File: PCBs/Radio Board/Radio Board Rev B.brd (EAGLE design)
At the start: 95.9 x 90.2 mm, 10 parts

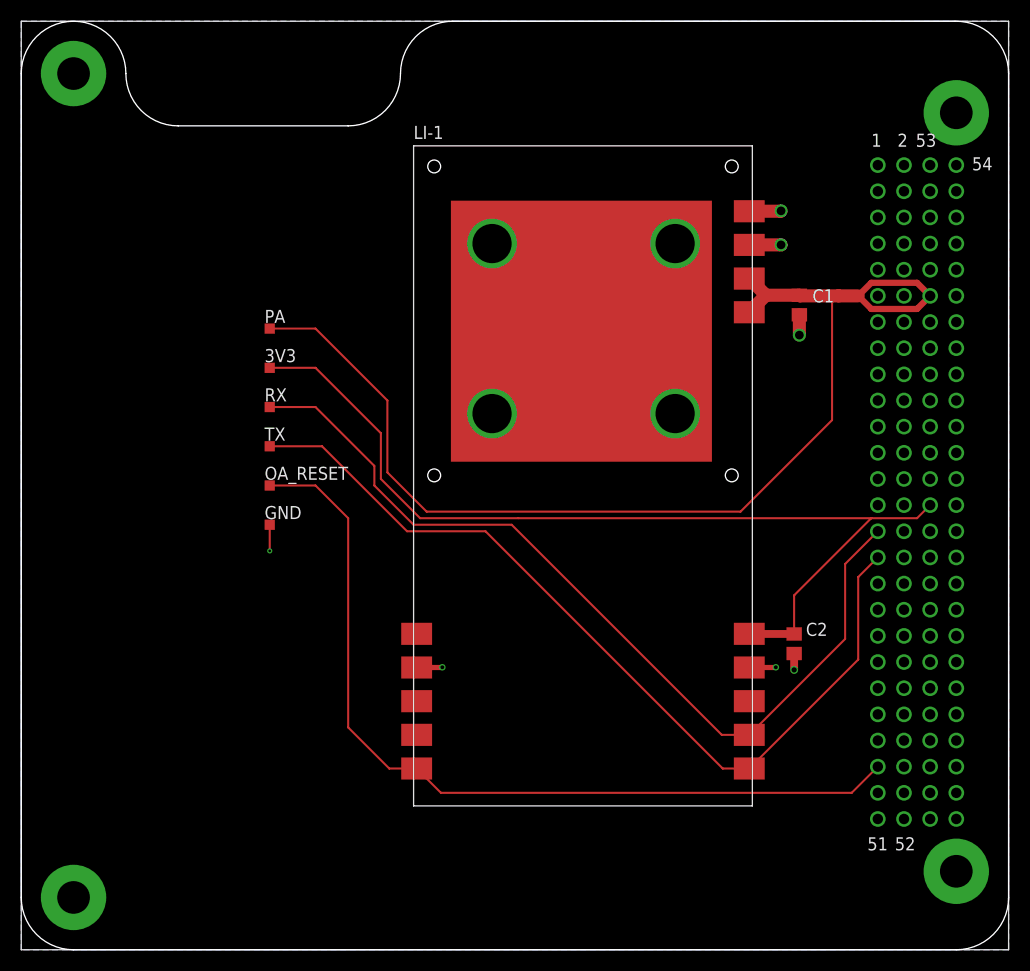
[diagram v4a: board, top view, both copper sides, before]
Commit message: Add Molex connector and connector bypass to radio board
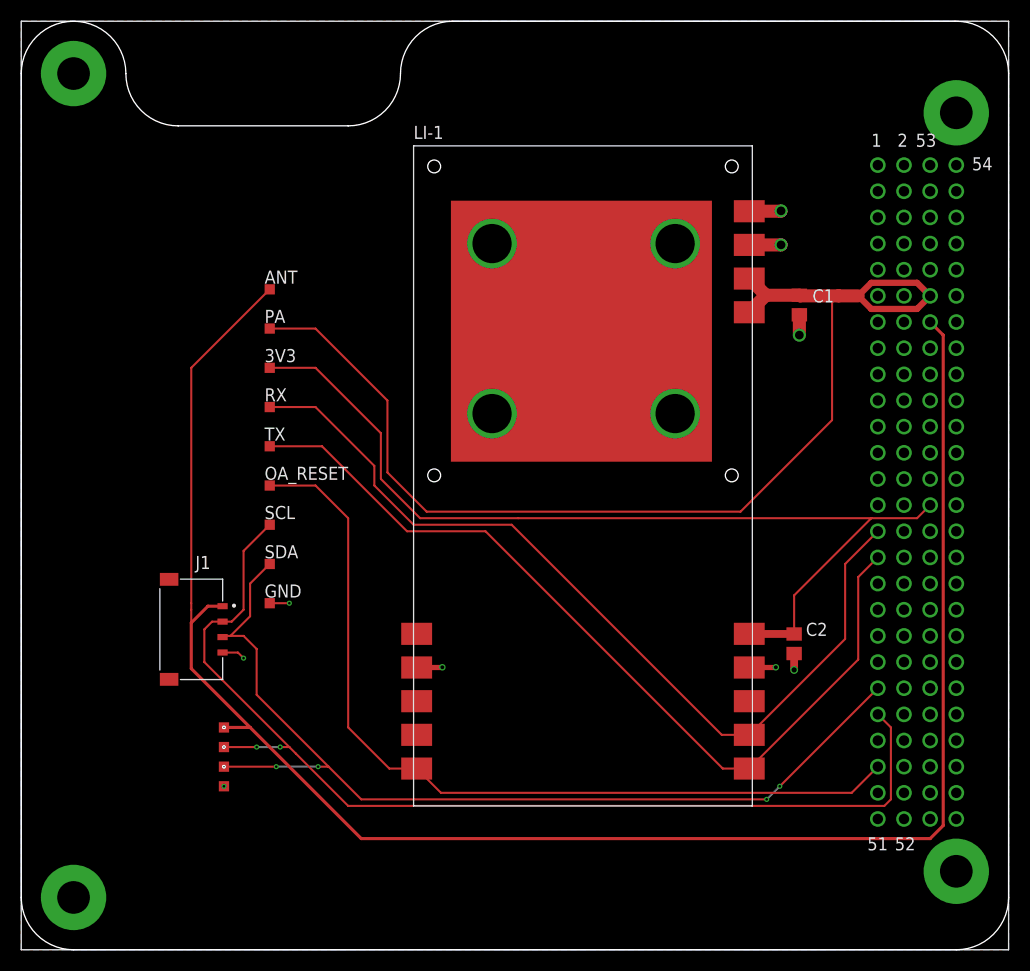
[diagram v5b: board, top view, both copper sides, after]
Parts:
- added ANT, J1_1, J1_2, J1_3, J1_4, SCL, SDA: TPTP10SQ, testpad:TP10SQ
- added J1: MOLEX_504050-0491, Molex 504050-0491:MOLEX_5040500491
- moved GND 7.62 mm to (24.1, 33.7)
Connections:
- new net SCL: J1.2, J1_2.TP, SCL.TP, U$1.43
- new net SDA: J1.3, J1_3.TP, SDA.TP, U$1.41
- new net SHIELD: J1.SH1, J1.SH2
- new net SW5: ANT.TP, J1.1, J1_1.TP, U$1.65
- net GND: now also J1.4, J1_4.TP
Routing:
- net SW5: track 0.00 -> 176.0 mm
- net SCL: track 0.00 -> 104.9 mm, vias 0 -> 2
- net SDA: track 0.00 -> 96.1 mm, vias 0 -> 4
- net GND: track 17.4 -> 19.0 mm, vias 7 -> 9
